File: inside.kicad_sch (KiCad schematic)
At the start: 13 parts, among them J1 Molex 0510211000, J2 Molex 0532611071, J3 Molex 0510211000, J4 Conn_01x06_Pin, J5 Conn_01x06_Pin, U1 MICROSD_SPI_OR_SDIO_CARD, U2 3073, U3 2472

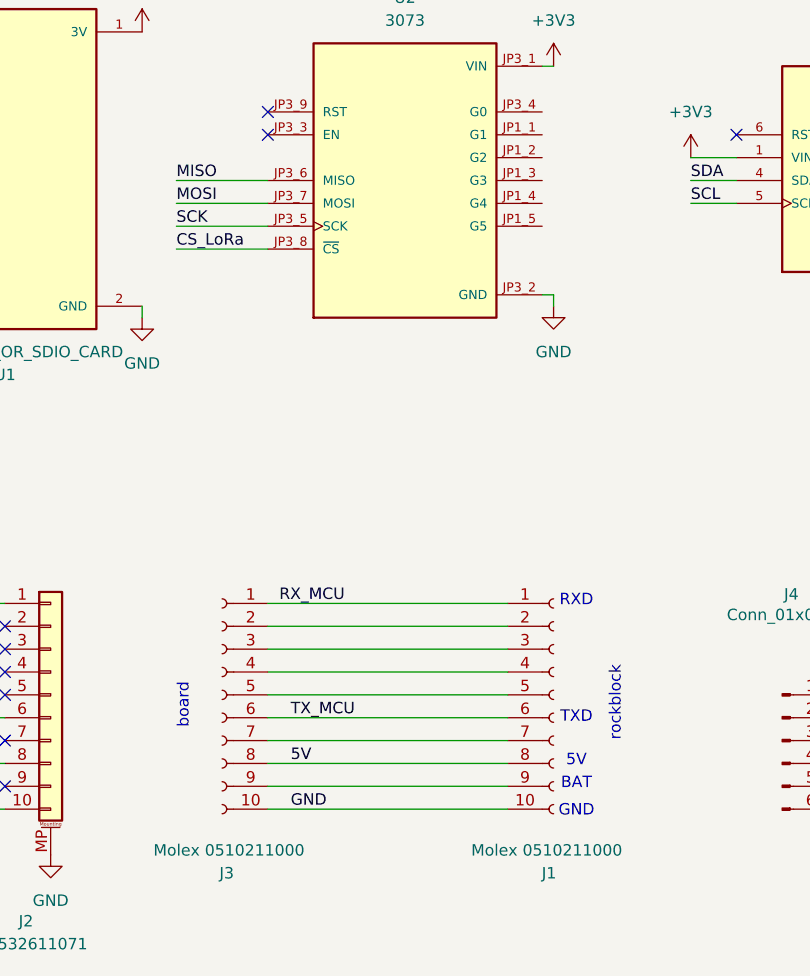
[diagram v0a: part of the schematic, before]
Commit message: added footprints
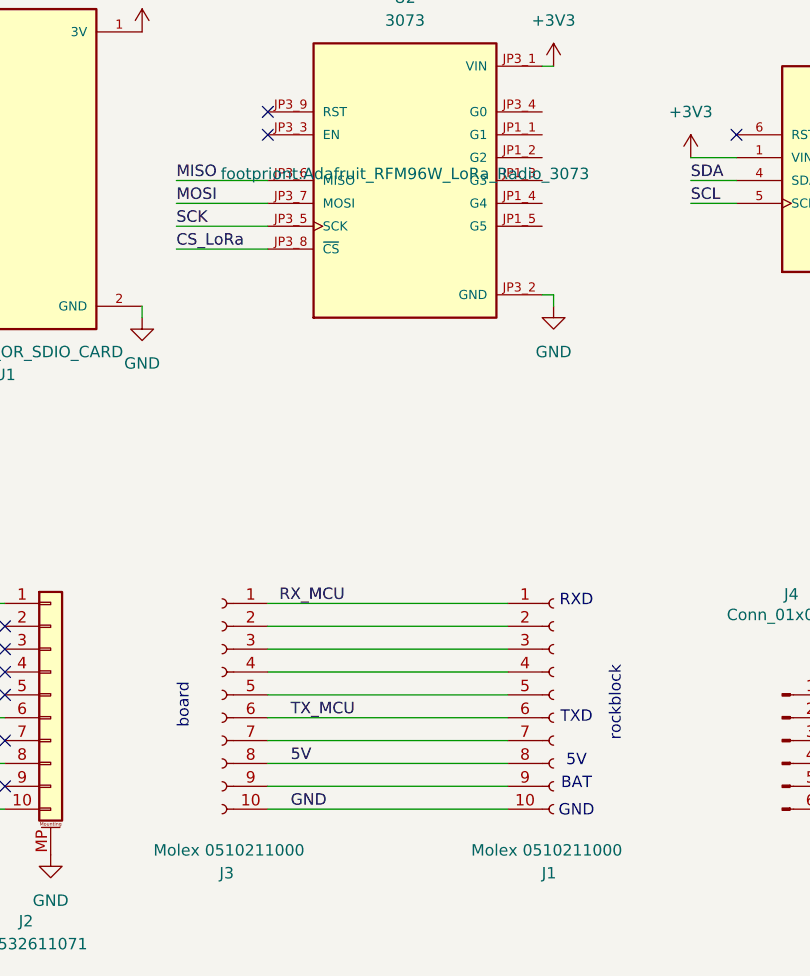
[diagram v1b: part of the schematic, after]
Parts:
- U2: footprint 3073:MODULE_3073 -> footpriont:Adafruit_RFM96W_LoRa_Radio_3073
- U3: footprint 2472:MODULE_2472 -> footpriont:adafruit_IMU_2472
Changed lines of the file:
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@@
 (kicad_sch
-	(version 20231120)
+	(version 20250114)
 	(generator "eeschema")
-	(generator_version "8.0")
+	(generator_version "9.0")
 	(paper "A4")
+	(text "RXD"
+		(exclude_from_sim no)
+		(at 130.81 110.236 0)
+		(effects
+			(font
+				(size 1.27 1.27)
+				(thickness 0.1588)
+			)
+		)
+	)
+	(text "rockblock"
+		(exclude_from_sim no)
+		(at 84.836 153.67 0)
+		(effects
+			(font
+				(size 2.54 2.54)
+				(thickness 0.254)
+				(bold yes)
+			)
+		)
+	)
+	(text "microsd"
+		(exclude_from_sim no)
+		(at 67.818 39.116 0)
+		(effects
+			(font
+				(size 2.54 2.54)
+				(thickness 0.254)
+				(bold yes)
+			)
+		)
+	)
+	(text "5V"
+		(exclude_from_sim no)
+		(at 130.81 128.016 0)
+		(effects
+			(font
+				(size 1.27 1.27)
+				(thickness 0.1588)
+			)
+		)
+	)
+	(text "IMU"
+		(exclude_from_sim no)
+		(at 163.576 41.656 0)
+		(effects
+			(font
+				(size 2.54 2.54)
+				(thickness 0.254)
+				(bold yes)
+			)
+		)
+	)
+	(text "BAT"
+		(exclude_from_sim no)
+		(at 130.81 130.556 0)
+		(effects
+			(font
+				(size 1.27 1.27)
+				(thickness 0.1588)
+			)
+		)
+	)
+	(text "board"
+		(exclude_from_sim no)
+		(at 87.122 121.92 90)
+		(effects
+			(font
+				(size 1.27 1.27)
+				(thickness 0.1588)
+			)
+		)
+	)
+	(text "GPS\n"
+		(exclude_from_sim no)
+		(at 164.338 140.97 0)
+		(effects
+			(font
+				(size 2.032 2.032)
+				(thickness 0.254)
+				(bold yes)
+			)
+		)
+	)
+	(text "LoRa"
+		(exclude_from_sim no)
+		(at 112.014 38.862 0)
+		(effects
+			(font
+				(size 2.54 2.54)
+				(thickness 0.254)
+				(bold yes)
+			)
+		)
+	)
+	(text "rockblock"
+		(exclude_from_sim no)
+		(at 135.128 121.666 90)
+		(effects
+			(font
+				(size 1.27 1.27)
+				(thickness 0.1588)
+			)
+		)
+	)
+	(text "GND\n"
+		(exclude_from_sim no)
+		(at 130.81 133.604 0)
+		(effects
+			(font
+				(size 1.27 1.27)
+				(thickness 0.1588)
+			)
+		)
+	)
+	(text "TXD"
+		(exclude_from_sim no)
+		(at 130.81 123.19 0)
+		(effects
+			(font
+				(size 1.27 1.27)
+				(thickness 0.1588)
+			)
+		)
+	)
 	(junction
 		(at 194.31 95.25)
@@
 		)
 	)
-	(text "RXD"
-		(exclude_from_sim no)
-		(at 130.81 110.236 0)
-		(effects
-			(font
-				(size 1.27 1.27)
-				(thickness 0.1588)
-			)
-		)
-	)
-	(text "rockblock"
-		(exclude_from_sim no)
-		(at 84.836 153.67 0)
-		(effects
-			(font
-				(size 2.54 2.54)
-				(thickness 0.254)
-				(bold yes)
-			)
-		)
-	)
-	(text "microsd"
-		(exclude_from_sim no)
-		(at 67.818 39.116 0)
-		(effects
-			(font
-				(size 2.54 2.54)
-				(thickness 0.254)
-				(bold yes)
-			)
-		)
-	)
-	(text "5V"
-		(exclude_from_sim no)
-		(at 130.81 128.016 0)
-		(effects
-			(font
-				(size 1.27 1.27)
-				(thickness 0.1588)
-			)
-		)
-	)
-	(text "IMU"
-		(exclude_from_sim no)
-		(at 163.576 41.656 0)
-		(effects
-			(font
-				(size 2.54 2.54)
-				(thickness 0.254)
-				(bold yes)
-			)
-		)
-	)
-	(text "BAT"
-		(exclude_from_sim no)
-		(at 130.81 130.556 0)
-		(effects
-			(font
-				(size 1.27 1.27)
-				(thickness 0.1588)
-			)
-		)
-	)
-	(text "board"
-		(exclude_from_sim no)
-		(at 87.122 121.92 90)
-		(effects
-			(font
-				(size 1.27 1.27)
-				(thickness 0.1588)
-			)
-		)
-	)
-	(text "GPS\n"
-		(exclude_from_sim no)
-		(at 164.338 140.97 0)
-		(effects
-			(font
-				(size 2.032 2.032)
-				(thickness 0.254)
-				(bold yes)
-			)
-		)
-	)
-	(text "LoRa"
-		(exclude_from_sim no)
-		(at 112.014 38.862 0)
-		(effects
-			(font
-				(size 2.54 2.54)
-				(thickness 0.254)
-				(bold yes)
-			)
-		)
-	)
-	(text "rockblock"
-		(exclude_from_sim no)
-		(at 135.128 121.666 90)
-		(effects
-			(font
-				(size 1.27 1.27)
-				(thickness 0.1588)
-			)
-		)
-	)
-	(text "GND\n"
-		(exclude_from_sim no)
-		(at 130.81 133.604 0)
-		(effects
-			(font
-				(size 1.27 1.27)
-				(thickness 0.1588)
-			)
-		)
-	)
-	(text "TXD"
-		(exclude_from_sim no)
-		(at 130.81 123.19 0)
-		(effects
-			(font
-				(size 1.27 1.27)
-				(thickness 0.1588)
-			)
-		)
-	)
 	(label "MISO"
 		(at 38.1 64.77 0)
-		(fields_autoplaced yes)
 		(effects
 			(font
@@
 	(label "CS_microSD"
 		(at 38.1 72.39 0)
-		(fields_autoplaced yes)
 		(effects
 			(font
@@
 	(label "SCK"
 		(at 38.1 57.15 0)
-		(fields_autoplaced yes)
 		(effects
 			(font
@@
 	(label "TX_MCU"
 		(at 58.42 123.19 0)
-		(fields_autoplaced yes)
 		(effects
 			(font
@@
 	(label "GND"
 		(at 54.61 133.35 0)
-		(fields_autoplaced yes)
 		(effects
 			(font
@@
 	(label "TX_MCU"
 		(at 99.06 123.19 0)
-		(fields_autoplaced yes)
 		(effects
 			(font
@@
 	(label "MISO"
 		(at 205.74 91.44 0)
-		(fields_autoplaced yes)
 		(effects
 			(font
@@
 	(label "SCL"
 		(at 205.74 106.68 0)
-		(fields_autoplaced yes)
 		(effects
 			(font
@@
 	(label "SCK"
 		(at 205.74 86.36 0)
-		(fields_autoplaced yes)
 		(effects
 			(font
@@
 	(label "CS_LoRa"
 		(at 86.36 71.12 0)
-		(fields_autoplaced yes)
 		(effects
 			(font
@@
 	(label "GND"
 		(at 99.06 133.35 0)
-		(fields_autoplaced yes)
 		(effects
 			(font
@@
 	(label "MOSI"
 		(at 205.74 88.9 0)
-		(fields_autoplaced yes)
 		(effects
 			(font
@@
 	(label "MOSI"
 		(at 38.1 59.69 0)
-		(fields_autoplaced yes)
 		(effects
 			(font
@@
 	(label "SCL"
 		(at 165.1 128.27 180)
-		(fields_autoplaced yes)
 		(effects
 			(font
@@
 	(label "MISO"
 		(at 86.36 63.5 0)
-		(fields_autoplaced yes)
 		(effects
 			(font
@@
 	(label "MOSI"
 		(at 86.36 66.04 0)
-		(fields_autoplaced yes)
 		(effects
 			(font
@@
 	(label "5V"
 		(at 54.61 128.27 0)
-		(fields_autoplaced yes)
 		(effects
 			(font
@@
 	(label "CS_microSD"
 		(at 201.93 66.04 0)
-		(fields_autoplaced yes)
 		(effects
 			(font
@@
 	(label "RX_MCU"
 		(at 205.74 96.52 0)
-		(fields_autoplaced yes)
 		(effects
 			(font
@@
 	(label "SCK"
 		(at 86.36 68.58 0)
-		(fields_autoplaced yes)
 		(effects
 			(font
@@
 	(label "TX_MCU"
 		(at 205.74 99.06 0)
-		(fields_autoplaced yes)
 		(effects
 			(font
@@
 	(label "CS_LoRa"
 		(at 201.93 63.5 0)
-		(fields_autoplaced yes)
 		(effects
 			(font
@@
 	(label "5V"
 		(at 99.06 128.27 0)
-		(fields_autoplaced yes)
 		(effects
 			(font
@@
 	(label "SDA"
 		(at 205.74 104.14 0)
-		(fields_autoplaced yes)
 		(effects
 			(font
@@
 	(label "SDA"
 		(at 165.1 130.81 180)
-		(fields_autoplaced yes)
 		(effects
 			(font
@@
 	(label "SCL"
 		(at 143.51 66.04 0)
-		(fields_autoplaced yes)
 		(effects
 			(font
@@
 	(label "RX_MCU"
 		(at 58.42 110.49 0)
-		(fields_autoplaced yes)
 		(effects
 			(font
@@
 	(label "RX_MCU"
 		(at 97.79 110.49 0)
-		(fields_autoplaced yes)
 		(effects
 			(font
@@
 	(label "SDA"
 		(at 143.51 63.5 0)
-		(fields_autoplaced yes)
 		(effects
 			(font
@@
 			)
 		)
-		(property "Footprint" "2472:MODULE_2472"
+		(property "Footprint" "footpriont:adafruit_IMU_2472"
 			(at 163.83 63.5 0)
 			(effects
@@
 			)
 		)
-		(property "Footprint" "3073:MODULE_3073"
+		(property "Footprint" "footpriont:Adafruit_RFM96W_LoRa_Radio_3073"
 			(at 111.76 63.5 0)
 			(effects
@@
 				)
 				(justify bottom)
-				(hide yes)
 			)
 		)

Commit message: Update schematic and PCB
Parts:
- H1, H2: footprint (none) -> MountingHole:MountingHole_3.2mm_M3
- J1, J3: footprint (none) -> Connector_Molex:Molex_PicoBlade_53047-1010_1x10_P1.25mm_Vertical
- J2: footprint (none) -> footprints-extra:CONN_532610001-SD_10_MOL
- J4, J5: footprint (none) -> Connector_Molex:Molex_PicoBlade_53047-0610_1x06_P1.25mm_Vertical
- R1, R2: footprint (none) -> Resistor_SMD:R_0603_1608Metric
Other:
- title: (none) -> Balloon Paylaod 
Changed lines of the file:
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@@
 	(generator_version "9.0")
 	(paper "A4")
+	(title_block
+		(title "Balloon Paylaod ")
+		(date "2025-07-29")
+	)
 	(text "RXD"
 		(exclude_from_sim no)
@@
 			)
 		)
-		(property "Footprint" ""
+		(property "Footprint" "Resistor_SMD:R_0603_1608Metric"
 			(at 195.326 103.124 90)
 			(effects
@@
 			)
 		)
-		(property "Footprint" ""
+		(property "Footprint" "Connector_Molex:Molex_PicoBlade_53047-1010_1x10_P1.25mm_Vertical"
 			(at 128.27 120.65 0)
 			(effects
@@
 			)
 		)
-		(property "Footprint" ""
+		(property "Footprint" "Connector_Molex:Molex_PicoBlade_53047-0610_1x06_P1.25mm_Vertical"
 			(at 172.72 125.73 0)
 			(effects
@@
 			)
 		)
-		(property "Footprint" ""
+		(property "Footprint" "Connector_Molex:Molex_PicoBlade_53047-1010_1x10_P1.25mm_Vertical"
 			(at 91.44 120.65 0)
 			(effects
@@
 			)
 		)
-		(property "Footprint" ""
+		(property "Footprint" "Connector_Molex:Molex_PicoBlade_53047-0610_1x06_P1.25mm_Vertical"
 			(at 153.67 125.73 0)
 			(effects
@@
 			)
 		)
-		(property "Footprint" ""
+		(property "Footprint" "Resistor_SMD:R_0603_1608Metric"
 			(at 199.136 100.584 90)
 			(effects
@@
 			)
 		)
-		(property "Footprint" ""
+		(property "Footprint" "footprints-extra:CONN_532610001-SD_10_MOL"
 			(at 72.39 120.65 0)
 			(effects
@@
 			)
 		)
-		(property "Footprint" ""
+		(property "Footprint" "MountingHole:MountingHole_3.2mm_M3"
 			(at 33.02 124.46 0)
 			(effects
@@
 			)
 		)
-		(property "Footprint" ""
+		(property "Footprint" "MountingHole:MountingHole_3.2mm_M3"
 			(at 33.02 116.84 0)
 			(effects

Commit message: "finished breakout version"
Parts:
- added H3: MountingHole, MountingHole:MountingHole_3.2mm_M3, symbol Mechanical:MountingHole
- added J6: USB_B_Micro, Connector_USB:USB_Micro-AB_Molex_47590-0001, symbol Connector:USB_B_Micro
- J1, J3: footprint Connector_Molex:Molex_PicoBlade_53047-1010_1x10_P1.25mm_Vertical -> (none)
- J2: footprint footprints-extra:CONN_532610001-SD_10_MOL -> Connector_Molex:Molex_PicoBlade_53398-1071_1x10-1MP_P1.25mm_Vertical
- J4, J5: footprint Connector_Molex:Molex_PicoBlade_53047-0610_1x06_P1.25mm_Vertical -> Connector_PinHeader_2.54mm:PinHeader_1x06_P2.54mm_Vertical
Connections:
- net +5V: now also J6.1 (VBUS)
- net GND: now also J6.5 (GND), J6.6 (Shield)
- no-connect marks 26 -> 29

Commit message: small tweaks
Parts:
- removed J6: USB_B_Micro, Connector_USB:USB_Micro-AB_Molex_47590-0001, symbol Connector:USB_B_Micro
- added H4, H5: MountingHole, MountingHole:MountingHole_2.7mm_M2.5, symbol Mechanical:MountingHole
- added X1: ~, Connector_JST:JST_PH_S2B-PH-SM4-TB_1x02-1MP_P2.00mm_Horizontal, symbol externalLib:CON_JST_PH_2PIN
- R1, R2: footprint Resistor_SMD:R_0603_1608Metric -> Resistor_THT:R_Axial_DIN0204_L3.6mm_D1.6mm_P5.08mm_Horizontal
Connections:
- net +5V: now also X1.2
- net GND: now also J4.2 (Pin_2), X1.1
- no-connect marks 29 -> 25
